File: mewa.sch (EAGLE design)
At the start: 63 parts, among them IC1 TL072D, IC2 TL072D, IC3 TL072D, IC4 TL072D, J1 STEREOSW, J2 STEREOSW, J3 STEREOSW, J4 STEREOSW, T1 PDTA114ET, T2 PDTA114ET, T3 BC847, T4 BC847

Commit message: Added DC/DC converters & voltage inverter
& changed analog ground to AGND
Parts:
- added C21, C22, C26, C32, C33, C34, C35, C36, C37: 100n, rcl:C-EUC0805
- added C23: 470u, rcl:CPOL-EUE2.5-7
- added C24, C25: 100u, rcl:CPOL-EUE2.5-7
- added C27: 10u, rcl:CPOL-EUE2.5-7
- added C28, C29: 10u, rcl:CPOL-EUE2,5-6E
- added C30, C31: 1u FILM, rcl:C-EUC0805
- added IC5: CS4270-CZZR, CS4270-CZZR:CS4270-CZZR
- added IC6: ICL7660CSA, maxim:ICL7660CSA
- added L1, L2, L3: 100u, rcl:L-EU0207/10
- added SJ1: SOLDERJUMPERPTH, SparkFun-Retired:SOLDERJUMPERPTH
- added U$1, U$2: DC/DC_MODULE, DEEP_MainBoard — kopia:DC/DC_MODULE
- R19: value 8.2k -> 100k
- renumbered J5 to 9V_CONN
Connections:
- removed net +3V3: R7.2
- new net +3.3V: C35.1, C36.1, C37.1, R7.2, U$2.OUT+
- new net +5V: C32.1, C33.1, C34.1, U$1.OUT+
- new net +9V: 9V_CONN.PIN, C21.1, C23.+, L1.1, U$1.IN+, U$2.IN+
- new net AGND: C12.1, C14.1, C15.1, C16.1, C17.1, C19.1, C2.1, C25.-, C26.2, C4.1, C5.1, C8.1, IC2A.+IN, J1.R, J1.S, J1.TN, J2.R, J2.S, J3.S, J4.S, JP1.1, JP2.3, JP3.3, JP4.3, JP5.3, R16.1, R19.1, R20.1, R21.1, R6.1, SJ1.1, T3.E, T4.E
- new net N$27: C27.+, IC6.CAP+
- new net N$28: C27.-, IC6.CAP-
- new net N$30: C28.-, C30.1, IC6.VOUT, L3.1
- new net V+: C22.1, C24.+, IC6.V+, L1.2, L2.1
- net #MUTEA: now also IC5.!MUTEA
- net #MUTEB: now also IC5.!MUTEB
- net +AVCC: now also C25.+, C26.1, L2.2
- net -AVCC: now also C29.-, C31.1, L3.2
- net CODEC_IN_A: now also IC5.AINA
- net CODEC_IN_B: now also IC5.AINB
- net CODEC_OUT_A: now also IC5.AOUTA
- net CODEC_OUT_B: now also IC5.AOUTB
- net GND: now also 9V_CONN.SLEEVE, C21.2, C22.2, C23.-, C24.-, C28.+, C29.+, C30.2, C31.2, C32.2, C33.2, C34.2, C35.2, C36.2, C37.2, IC6.GND, SJ1.2, U$1.IN-, U$1.OUT-, U$2.IN-, U$2.OUT-; no longer C12.1, C14.1, C15.1, C16.1, C17.1, C19.1, C2.1, C4.1, C5.1, C8.1, IC2A.+IN, J1.R, J1.S, J1.TN, J2.R, J2.S, J3.S, J4.S, JP1.1, JP2.3, JP3.3, JP4.3, JP5.3, R16.1, R19.1, R20.1, R21.1, R6.1, T3.E, T4.E
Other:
- note added: "3.3V DC/DC Step Down"
- note added: "5V & 3.3V STEP DOWN CONVERTERS"
- note added: "5V DC/DC Step Down"
- note added: "POWER FILTER & VOLTAGE INVERTER"

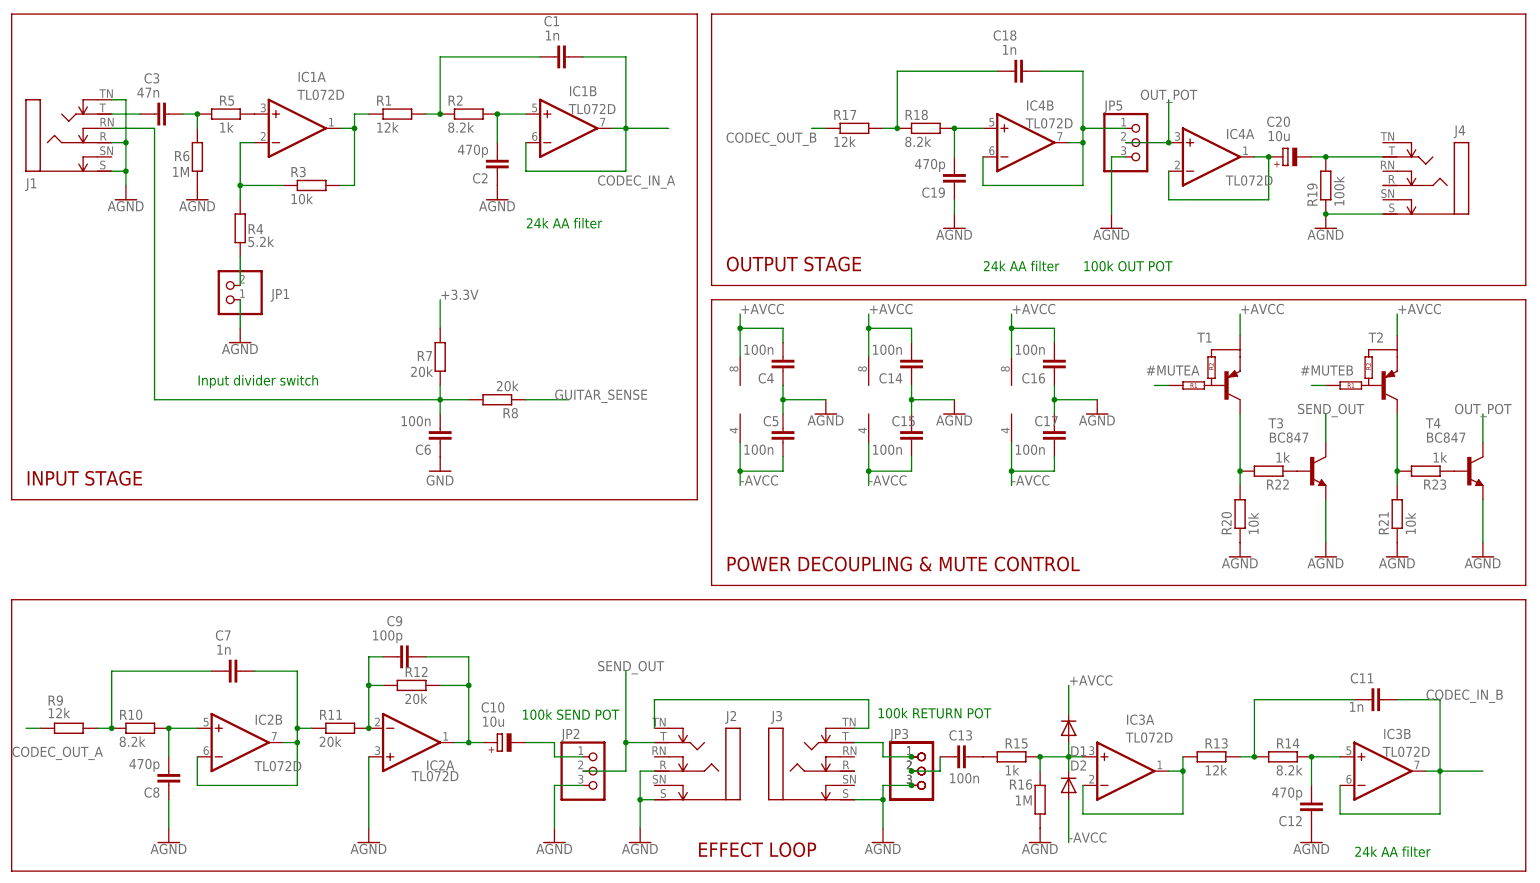
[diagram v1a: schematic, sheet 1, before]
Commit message: Fixed ADC signal levels, added testpads
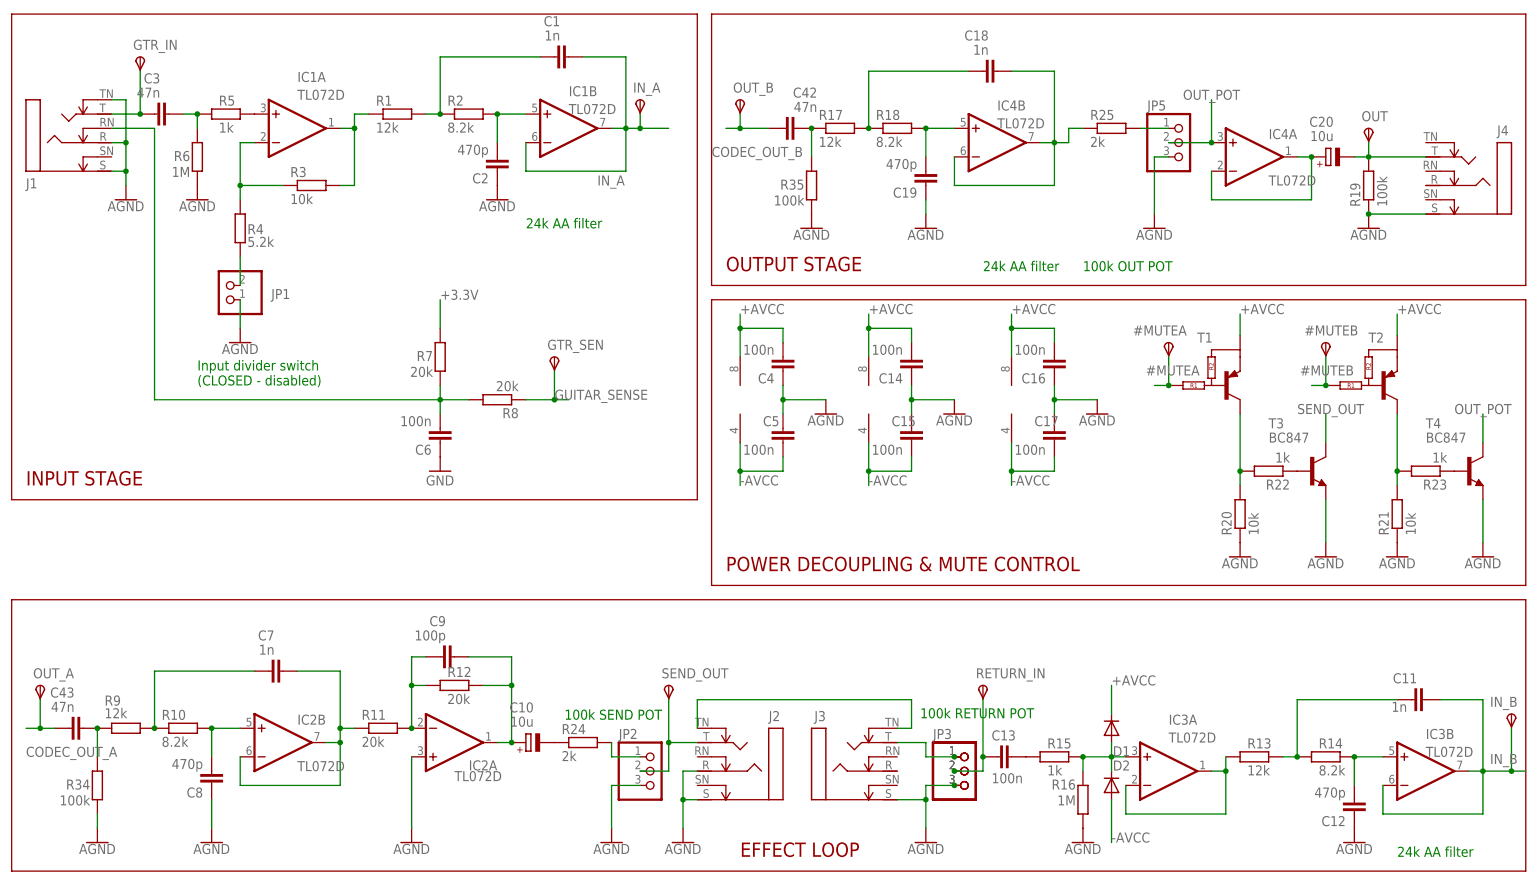
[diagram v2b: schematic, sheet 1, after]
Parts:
- added #MUTEA, #MUTEB, -AVCC, 3.3V, 5V, 5VA, 9V, AGND, AVCC, GND, GTR_IN, GTR_SEN, IN_A, IN_B, OUT, OUT_A, OUT_B, RETURN_IN, SEND_OUT, V+: TPSTP20R, testpad:TPSTP20R
- added C38: 100u, rcl:CPOL-EUE2.5-7
- added C39: 100n, rcl:C-EUC0805
- added C40, C41: 220n, rcl:C-EUC0805
- added C42, C43: 47n, rcl:C-EUC0805
- added D3, D4, D5, D6: PMLL4148L, NXP_60_26022015:PMLL4148L
- added L4: 100u, rcl:L-EU0207/10
- added R24, R25: 2k, rcl:R-EU_M0805
- added R26, R28: 68k, rcl:R-EU_M0805
- added R27, R29: 20k, rcl:R-EU_M0805
- added R30, R31, R32, R33: 1k, rcl:R-EU_M0805
- added R34, R35: 100k, rcl:R-EU_M0805
- renumbered U$1 to 5VCONV, U$2 to 3V3CONV
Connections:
- new net +5VA: 5VA.PP, C38.+, C39.1, D3.K, D5.K, L4.2, R26.2, R28.2
- new net IN_A: C1.2, C40.1, IC1B.-IN, IC1B.OUT, IN_A.PP
- new net IN_B: C11.2, C41.1, IC3B.-IN, IC3B.OUT, IN_B.PP
- new net IN_CODEC_A: R30.1
- new net IN_CODEC_B: R31.1
- new net N$16: C10.-, R24.1
- new net N$33: JP5.1, R25.2
- new net N$34: C42.2, R17.1, R35.2
- new net N$37: C43.2, R34.2, R9.1
- new net N$38: D3.A, D4.K, R26.1, R27.2, R30.2, R33.1
- new net N$39: C41.2, R32.2
- new net N$40: C40.2, R33.2
- new net N$41: D5.A, D6.K, R28.1, R29.2, R31.2, R32.1
- net #MUTEA: now also #MUTEA.PP
- net #MUTEB: now also #MUTEB.PP
- net +3.3V: now also 3.3V.PP
- net +5V: now also 5V.PP, L4.1
- net +9V: now also 9V.PP
- net +AVCC: now also AVCC.PP
- net -AVCC: now also -AVCC.PP
- net AGND: now also AGND.PP, C38.-, C39.2, D4.A, D6.A, R27.1, R29.1, R34.1, R35.1
- net CODEC_IN_A: no longer C1.2, IC1B.-IN, IC1B.OUT
- net CODEC_IN_B: no longer C11.2, IC3B.-IN, IC3B.OUT
- net CODEC_OUT_A: now also C43.1, OUT_A.PP; no longer R9.1
- net CODEC_OUT_B: now also C42.1, OUT_B.PP; no longer R17.1
- net GND: now also GND.PP
- net GUITAR_SENSE: now also GTR_SEN.PP
- net N$14: now also R24.2; no longer C10.-
- net N$23: now also RETURN_IN.PP
- net N$26: now also OUT.PP
- net N$9: now also GTR_IN.PP
- net SEND_OUT: now also SEND_OUT.PP
- net TT: now also R25.1; no longer JP5.1
- net V+: now also V+.PP
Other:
- note added: "Input divider switch (CLOSED - disabled)"
- note added: "SIGNAL SHIFTER & INPUT PROTECTION"
- note removed: "Input divider switch"
- moved on the sheet: C10, C11, C12, C13, C18, C19, C20, C7, C8, C9, D1, D2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

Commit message: AA filters topology changed to Bessel, fc=20kHz
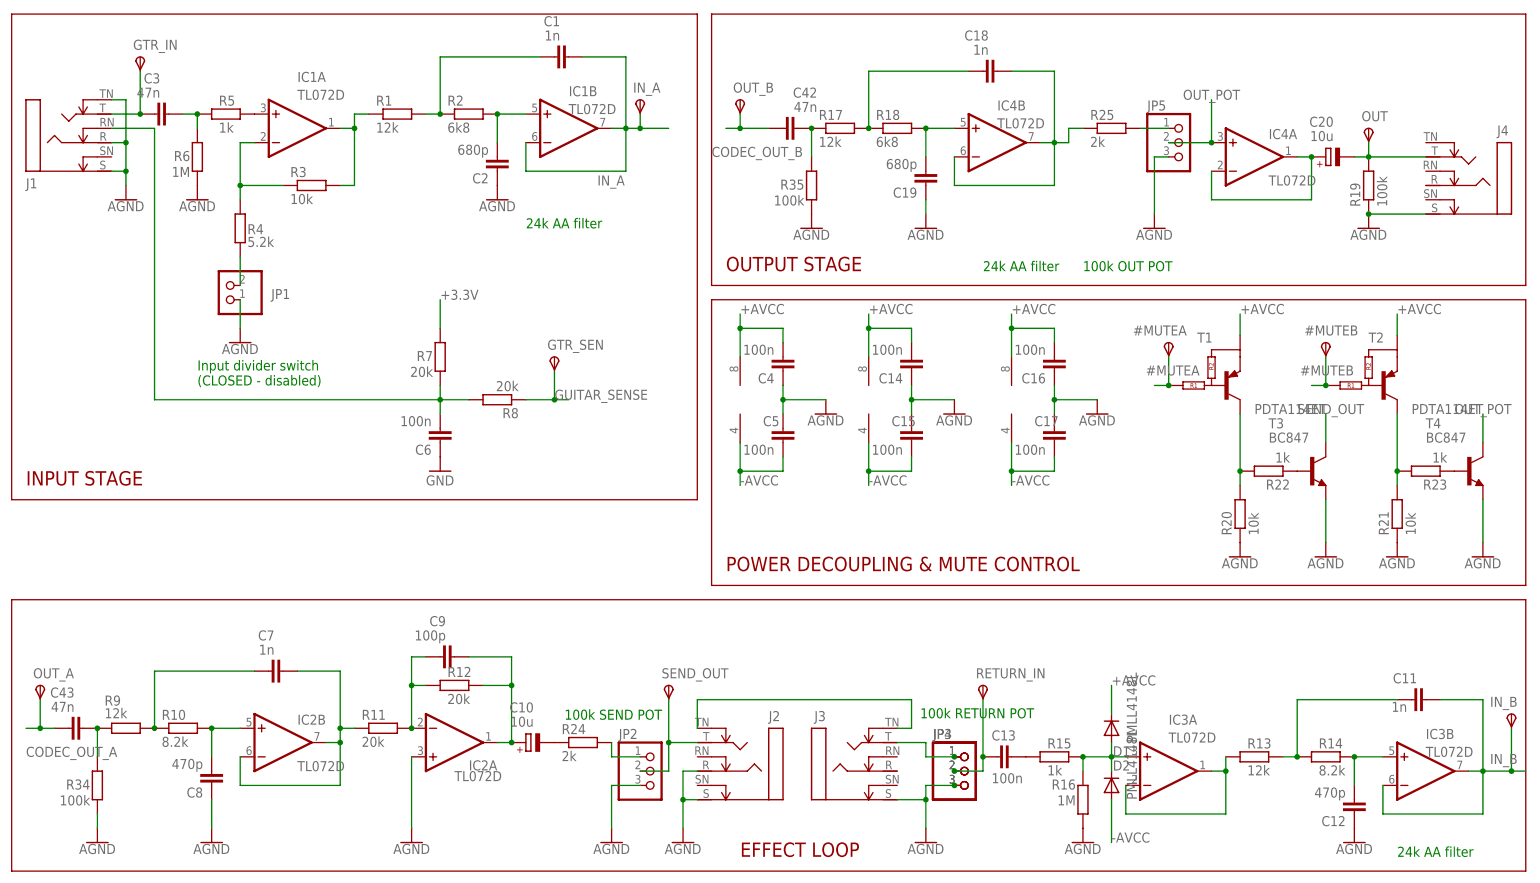
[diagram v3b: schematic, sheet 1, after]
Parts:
- C19, C2: value 470p -> 680p
- R18, R2: value 8.2k -> 6k8

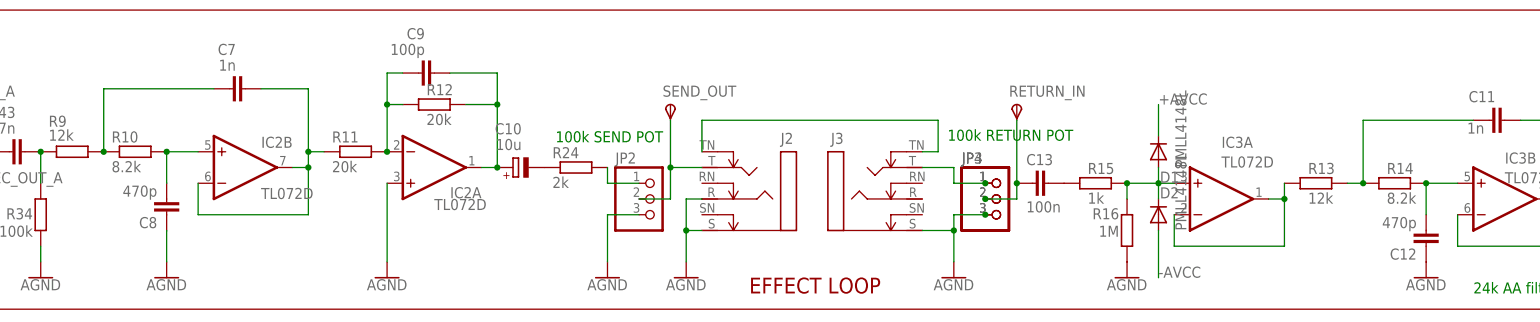
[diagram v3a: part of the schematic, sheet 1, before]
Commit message: AA in FX loop changed also
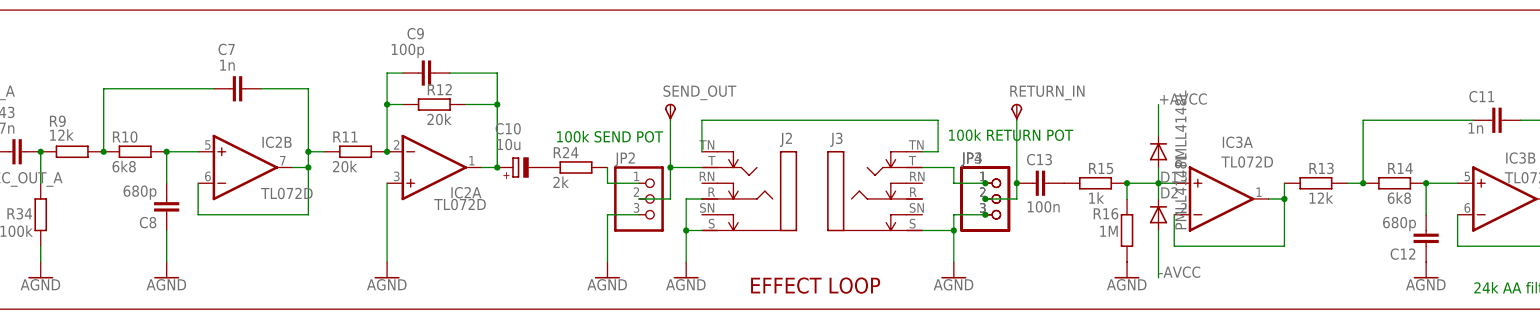
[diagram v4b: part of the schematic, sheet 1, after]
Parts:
- C12, C8: value 470p -> 680p
- R10, R14: value 8.2k -> 6k8
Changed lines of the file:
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@@
 <part name="IC2" library="linear" library_urn="urn:adsk.eagle:library:262" deviceset="TL072" device="D" package3d_urn="urn:adsk.eagle:package:16404/2"/>
 <part name="R9" library="rcl" library_urn="urn:adsk.eagle:library:334" deviceset="R-EU_" device="M0805" package3d_urn="urn:adsk.eagle:package:23556/2" value="12k"/>
-<part name="R10" library="rcl" library_urn="urn:adsk.eagle:library:334" deviceset="R-EU_" device="M0805" package3d_urn="urn:adsk.eagle:package:23556/2" value="8.2k"/>
+<part name="R10" library="rcl" library_urn="urn:adsk.eagle:library:334" deviceset="R-EU_" device="M0805" package3d_urn="urn:adsk.eagle:package:23556/2" value="6k8"/>
 <part name="C7" library="rcl" library_urn="urn:adsk.eagle:library:334" deviceset="C-EU" device="C0805" package3d_urn="urn:adsk.eagle:package:23617/2" value="1n"/>
-<part name="C8" library="rcl" library_urn="urn:adsk.eagle:library:334" deviceset="C-EU" device="C0805" package3d_urn="urn:adsk.eagle:package:23617/2" value="470p"/>
+<part name="C8" library="rcl" library_urn="urn:adsk.eagle:library:334" deviceset="C-EU" device="C0805" package3d_urn="urn:adsk.eagle:package:23617/2" value="680p"/>
 <part name="R11" library="rcl" library_urn="urn:adsk.eagle:library:334" deviceset="R-EU_" device="M0805" package3d_urn="urn:adsk.eagle:package:23556/2" value="20k"/>
 <part name="R12" library="rcl" library_urn="urn:adsk.eagle:library:334" deviceset="R-EU_" device="M0805" package3d_urn="urn:adsk.eagle:package:23556/2" value="20k"/>
@@
 <part name="IC3" library="linear" library_urn="urn:adsk.eagle:library:262" deviceset="TL072" device="D" package3d_urn="urn:adsk.eagle:package:16404/2"/>
 <part name="R13" library="rcl" library_urn="urn:adsk.eagle:library:334" deviceset="R-EU_" device="M0805" package3d_urn="urn:adsk.eagle:package:23556/2" value="12k"/>
-<part name="R14" library="rcl" library_urn="urn:adsk.eagle:library:334" deviceset="R-EU_" device="M0805" package3d_urn="urn:adsk.eagle:package:23556/2" value="8.2k"/>
+<part name="R14" library="rcl" library_urn="urn:adsk.eagle:library:334" deviceset="R-EU_" device="M0805" package3d_urn="urn:adsk.eagle:package:23556/2" value="6k8"/>
 <part name="C11" library="rcl" library_urn="urn:adsk.eagle:library:334" deviceset="C-EU" device="C0805" package3d_urn="urn:adsk.eagle:package:23617/2" value="1n"/>
-<part name="C12" library="rcl" library_urn="urn:adsk.eagle:library:334" deviceset="C-EU" device="C0805" package3d_urn="urn:adsk.eagle:package:23617/2" value="470p"/>
+<part name="C12" library="rcl" library_urn="urn:adsk.eagle:library:334" deviceset="C-EU" device="C0805" package3d_urn="urn:adsk.eagle:package:23617/2" value="680p"/>
 <part name="R15" library="rcl" library_urn="urn:adsk.eagle:library:334" deviceset="R-EU_" device="M0805" package3d_urn="urn:adsk.eagle:package:23556/2" value="1k"/>
 <part name="C13" library="rcl" library_urn="urn:adsk.eagle:library:334" deviceset="C-EU" device="C0805" package3d_urn="urn:adsk.eagle:package:23617/2" value="100n"/>
